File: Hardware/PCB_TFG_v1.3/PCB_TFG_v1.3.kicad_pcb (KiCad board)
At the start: 2 copper layers, 44.4 x 62 mm, 48 parts, among them J2 Conn_01x06_Pin, J3 770669-1, Q1 8MHz, Q3 NPN, U1 STM32H523CET6, U2 TCAN330, U3 MCP1755ST-3302E/DB

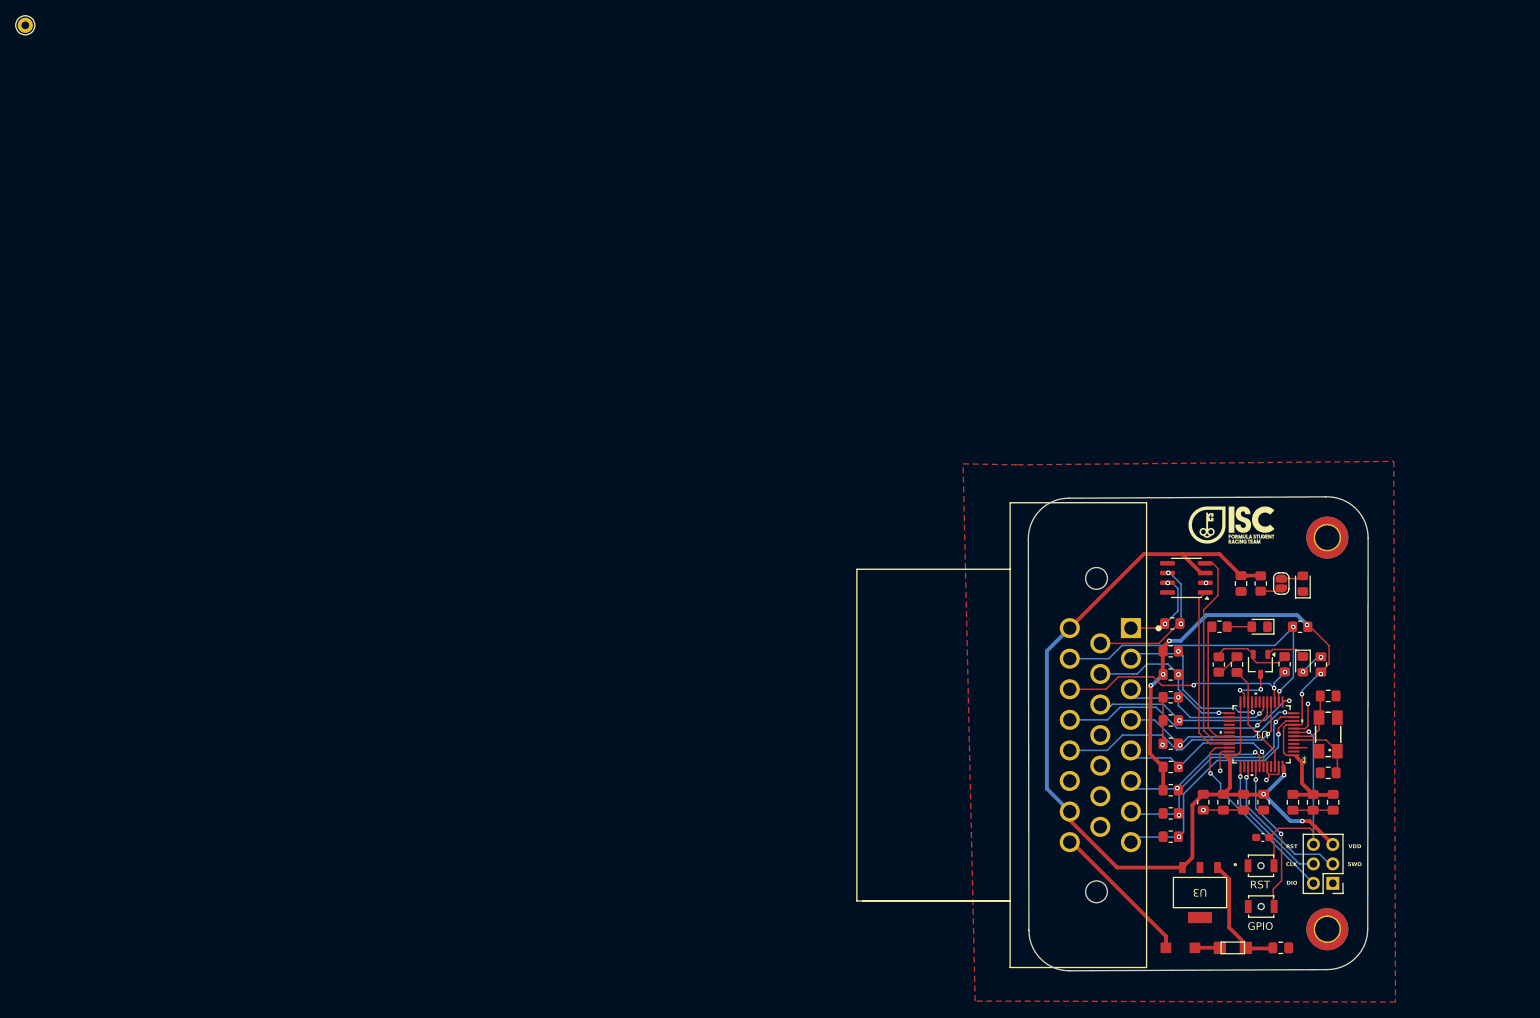
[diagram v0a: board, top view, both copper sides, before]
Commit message: MODIFICACIONES AL PCB
- Separación de Áreas Analógica y Digital.
- Creación de dos planos de GND y Vcc en capas intermedias.
- Recolocación de los C de desacoplo.
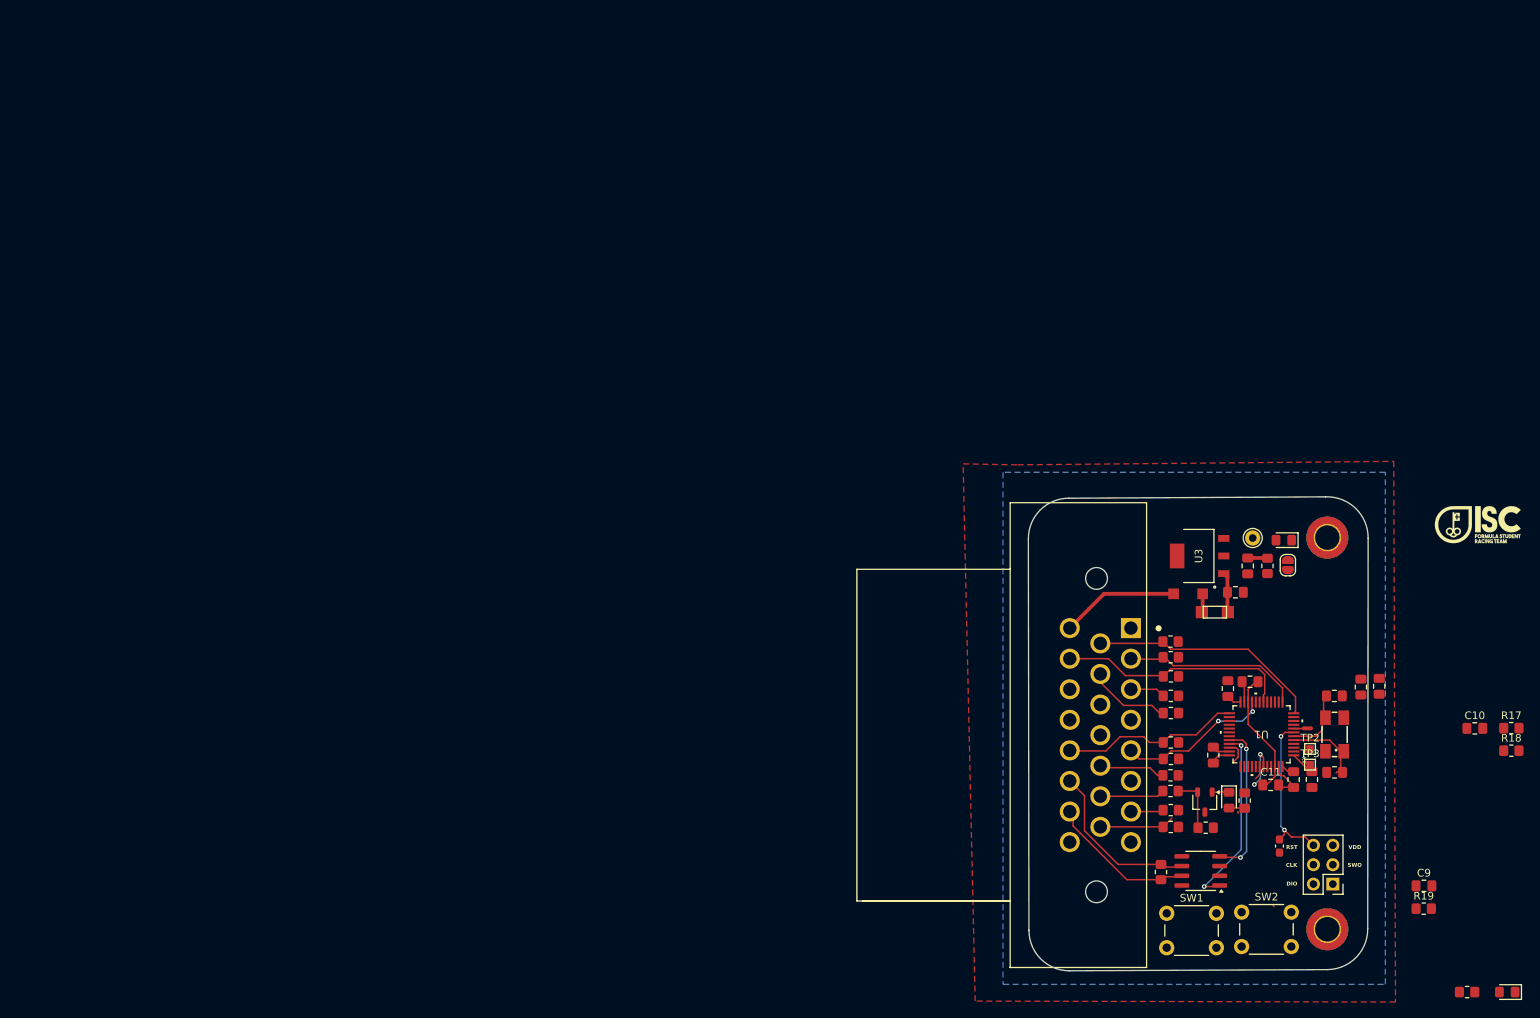
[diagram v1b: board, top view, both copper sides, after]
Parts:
- added C10: 2.2 uF, Capacitor_SMD:C_0805_2012Metric_Pad1.18x1.45mm_HandSolder, F.Cu at (201.7, 93.5)
- added C11: 2.2 uF, Capacitor_SMD:C_0805_2012Metric_Pad1.18x1.45mm_HandSolder, F.Cu at (175.0, 100.9)
- added NT1: NetTie_2, NetTie:NetTie-2_SMD_Pad0.5mm, F.Cu at (179.8, 93.5)
- added R17: 0, Resistor_SMD:R_0805_2012Metric_Pad1.20x1.40mm_HandSolder, F.Cu at (206.5, 93.5)
- added R18: 10k, Resistor_SMD:R_0805_2012Metric_Pad1.20x1.40mm_HandSolder, F.Cu at (206.5, 96.4)
- added R19: 100k, Resistor_SMD:R_0805_2012Metric_Pad1.20x1.40mm_HandSolder, F.Cu at (195.0, 117.1)
- added TP2: LSE_OSC_IN, TestPoint:TestPoint_Pad_1.0x1.0mm, F.Cu at (180.2, 96.2)
- added TP3: LSE_OSC_OUT, TestPoint:TestPoint_Pad_1.0x1.0mm, F.Cu at (180.2, 98.2)
- SW1: renamed from RST; footprint Button_Switch_SMD:SW_SPST_B3U-1000P-B -> Button_Switch_THT:SW_PUSH_6mm_H4.3mm
- SW2: renamed from GPIO; footprint Button_Switch_SMD:SW_SPST_B3U-1000P-B -> Button_Switch_THT:SW_PUSH_6mm_H4.3mm
- moved TP1 174.0 mm to (172.7, 68.6)
- moved D3 57.7 mm to (205.9, 128.0)
- moved R7 57.7 mm to (200.7, 128.0)
- moved C3 46.9 mm to (170.4, 75.7)
- moved D2 46.3 mm to (164.2, 75.9)
- moved U3 44.0 mm to (165.6, 71.0), turned to 90 degrees
- moved U$1 44.0 mm to (167.7, 78.3)
- moved U2 38.4 mm to (165.8, 112.2)
- moved R3 32.6 mm to (160.7, 112.3), turned to 90 degrees
- moved G*** 32.2 mm to (202.1, 66.8)
- moved C9 28.4 mm to (195.1, 114.1), turned to 0 degrees
- moved R16 25.8 mm to (161.9, 99.7)
- moved R12 22.3 mm to (161.9, 101.7), turned to 0 degrees
- moved R13 21.4 mm to (166.5, 106.5), turned to 0 degrees
- moved R14 20.4 mm to (171.6, 103.0), turned to 90 degrees
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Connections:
- C4 pad 2: GND -> unconnected-(C4-Pad2)
- C6 pad 2: VBAT -> VDDA
- C7 pad 2: VBAT -> VDDA
- D2 pad C: Net-(D2-PadC) -> unconnected-(D2-PadC)
- J3 pad 1: CANH1 -> GNDA
- J3 pad 10: TEMP_TYRE_2_SDA -> S_SUSP_FL
- J3 pad 11: APPS_2 -> unconnected-(J3-Pad11)
- J3 pad 13: unconnected-(J3-Pad13) -> TEMPS_BRK_CS
- J3 pad 14: unconnected-(J3-Pad14) -> TEMPS_BRK_SCK
- J3 pad 15: unconnected-(J3-Pad15) -> TEMP_TYRE_1_SDA
- J3 pad 16: VDD -> unconnected-(J3-Pad16)
- J3 pad 17: TEMPS_BRK_CS -> PRSS_BRK
- J3 pad 18: TEMPS_BRK_SCK -> unconnected-(J3-Pad18)
- J3 pad 19: TEMPS_BRK_MOSI -> unconnected-(J3-Pad19)
- J3 pad 2: TEMP_TYRE_2_SCL -> APPS_2
- J3 pad 20: TEMPS_BRK_MISO -> TEMP_TYRE_2_SDA
- J3 pad 21: unconnected-(J3-Pad21) -> CANL1
- J3 pad 22: VDD -> CANH1
- J3 pad 23: +12V -> VDD
- J3 pad 3: PRSS_BRK -> S_SUSP_FR
- J3 pad 4: APPS_1 -> TEMPS_BRK_MISO
- J3 pad 5: TEMP_TYRE_1_SDA -> TEMP_TYRE_2_SCL
- J3 pad 6: TEMP_TYRE_1_SCL -> TEMPS_BRK_MOSI
- J3 pad 7: S_SUSP_FR -> TEMP_TYRE_1_SCL
- J3 pad 8: S_SUSP_FL -> GND
- J3 pad 9: CANL1 -> APPS_1
- U$1 pad P$1: Net-(D2-PadC) -> unconnected-(U$1-PadP$1)
- U1 pad 3: unconnected-(U1-PC14-OSC32_IN-Pad3) -> Net-(U1-PC14-OSC32_IN)
- U1 pad 4: unconnected-(U1-PC15-OSC32_OUT-Pad4) -> Net-(U1-PC15-OSC32_OUT)
- U1 pad 44: GND -> Net-(SW3-B)
- U1 pad 46: Net-(C10-Pad1) -> Net-(C11-Pad1)
- U1 pad 8: GND -> GNDA
- U1 pad 9: VBAT -> VDDA
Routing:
- net VDD: track 128.3 -> 9.81 mm, vias 3 -> 0
- net VBAT: track 75.6 -> 2.95 mm, vias 6 -> 0
- net TEMPS_BRK_CS: track 41.6 -> 8.71 mm, vias 2 -> 0
- net TEMPS_BRK_MISO: track 32.8 -> 0.00 mm, vias 1 -> 0
- net TEMPS_BRK_MOSI: track 30.1 -> 0.00 mm, vias 1 -> 0
- net GND: track 40.6 -> 11.9 mm, vias 8 -> 0
- net S_SUSP_FR: track 31.3 -> 4.58 mm, vias 2 -> 0
- net TEMPS_BRK_SCK: track 34.0 -> 8.47 mm, vias 3 -> 0
- net SWDIO: track 26.0 -> 3.28 mm, vias 1 -> 0
- net S_SUSP_FL: track 33.6 -> 11.0 mm, vias 2 -> 0
- net GPIO: track 20.4 -> 0.18 mm, vias 2 -> 0
- net SWO: track 19.9 -> 0.00 mm, vias 1 -> 0
- net SWCLK: track 17.8 -> 0.51 mm, vias 1 -> 0
- net FLAG: track 16.7 -> 0.00 mm
- net TEMP_TYRE_1_SCL: track 21.7 -> 5.86 mm, vias 2 -> 0
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- added copper zone on B.Cu, net GND
- added copper zone on In2.Cu, net GND
- added copper zone on In1.Cu, net VDD
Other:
- copper layers 2 -> 4

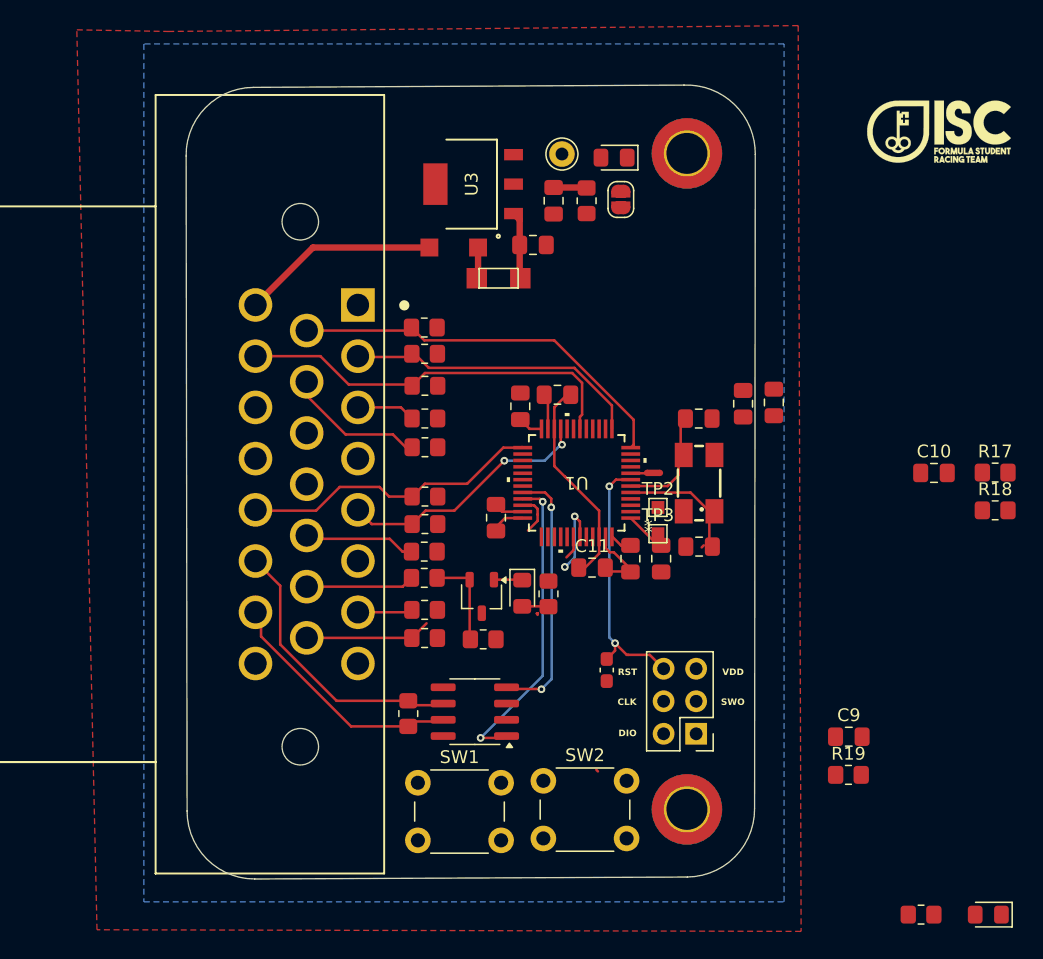
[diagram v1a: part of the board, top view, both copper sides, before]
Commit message: ENRUTADO COMPLETADO
- Nueva versión del PCB ya enrutado.
- Modificadas huellas de algunos componentes, principalmente para incluir marca de posición.
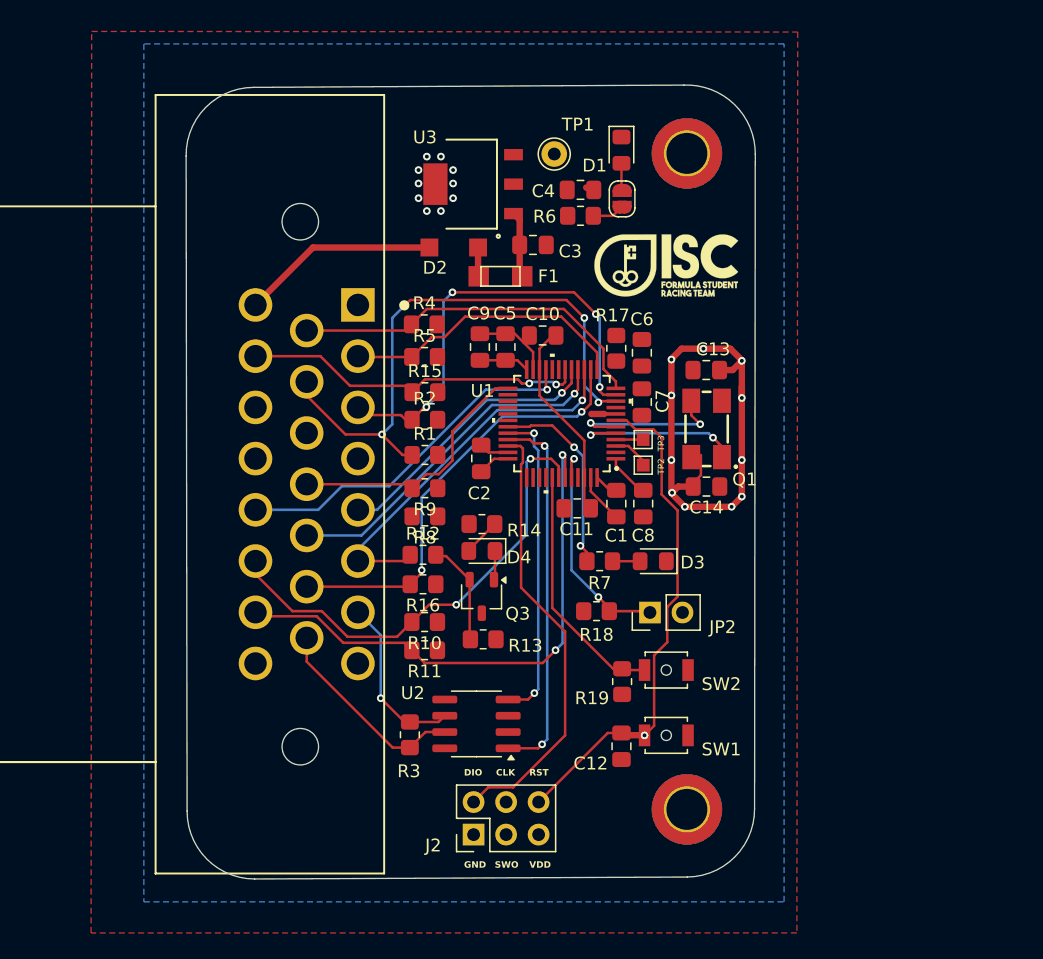
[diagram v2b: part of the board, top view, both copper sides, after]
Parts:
- removed the C10 at (172.3, 87.4)
- added JP2: Jumper_2_Open, Connector_PinHeader_2.54mm:PinHeader_1x02_P2.54mm_Vertical, F.Cu at (179.5, 104.4)
- C12: footprint Capacitor_SMD:C_0603_1608Metric_Pad1.08x0.95mm_HandSolder -> Capacitor_SMD:C_0805_2012Metric_Pad1.18x1.45mm_HandSolder
- SW1, SW2: footprint Button_Switch_THT:SW_PUSH_6mm_H4.3mm -> Button_Switch_SMD:SW_SPST_B3U-1000P-B
- moved C9 41.9 mm to (166.2, 83.7), turned to 90 degrees
- moved D3 38.0 mm to (179.8, 100.4)
- moved R7 37.3 mm to (175.6, 100.4)
- moved C10 32.4 mm to (171.1, 82.8), turned to 180 degrees
- moved R18 32.1 mm to (175.3, 104.3)
- moved R17 31.1 mm to (176.9, 83.8), turned to 90 degrees
- moved G*** 23.7 mm to (180.8, 77.3)
- moved SW1 19.7 mm to (180.8, 114.0), turned to 180 degrees
- moved R19 19.1 mm to (177.3, 109.8), turned to 90 degrees
- moved J2 19.1 mm to (165.8, 121.8), turned to 90 degrees
- moved SW2 12.9 mm to (180.8, 108.9), turned to 180 degrees
- moved C6 11.0 mm to (178.9, 84.1), turned to -90 degrees
- moved C7 7.91 mm to (178.9, 88.0)
- moved R14 7.53 mm to (166.4, 97.5), turned to 180 degrees
- moved TP3 7.44 mm to (179.0, 90.9)
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- renumbered U$1 to F1
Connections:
- C10 pad 1: Net-(C10-Pad1) -> VCAP
- C11 pad 1: Net-(C11-Pad1) -> VCAP
- C4 pad 2: unconnected-(C4-Pad2) -> GND
- C6 pad 1: GND -> GNDA
- C7 pad 1: GND -> GNDA
- D2 pad C: unconnected-(D2-PadC) -> Net-(D2-PadC)
- F1 pad P$1: unconnected-(U$1-PadP$1) -> Net-(D2-PadC)
- J3 pad 12: unconnected-(J3-Pad12) -> TEMP_TYRE_2_SDA
- J3 pad 13: TEMPS_BRK_CS -> TEMPS_BRK_MISO
- J3 pad 14: TEMPS_BRK_SCK -> TEMPS_BRK_CS
- J3 pad 15: TEMP_TYRE_1_SDA -> CANH1
- J3 pad 16: unconnected-(J3-Pad16) -> +12V
- J3 pad 20: TEMP_TYRE_2_SDA -> TEMP_TYRE_2_SCL
- J3 pad 21: CANL1 -> TEMP_TYRE_1_SCL
- J3 pad 22: CANH1 -> TEMP_TYRE_1_SDA
- J3 pad 4: TEMPS_BRK_MISO -> unconnected-(J3-Pad4)
- J3 pad 5: TEMP_TYRE_2_SCL -> TEMPS_BRK_MOSI
- J3 pad 6: TEMPS_BRK_MOSI -> TEMPS_BRK_SCK
- J3 pad 7: TEMP_TYRE_1_SCL -> CANL1
- U1 pad 22: Net-(C10-Pad1) -> VCAP
- U1 pad 46: Net-(C11-Pad1) -> VCAP
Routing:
- net GND: track 11.9 -> 53.6 mm, vias 0 -> 21
- net S_SUSP_FL: track 11.0 -> 45.3 mm, vias 0 -> 4
- net SWDIO: track 3.28 -> 34.4 mm
- net TEMP_TYRE_1_SCL: track 5.86 -> 36.9 mm, vias 0 -> 2
- net S_SUSP_FR: track 4.58 -> 35.3 mm, vias 0 -> 4
- net TEMPS_BRK_MISO: track 0.00 -> 27.9 mm, vias 0 -> 1
- net TEMP_TYRE_1_SDA: track 15.9 -> 43.4 mm
- net TEMPS_BRK_CS: track 8.71 -> 34.2 mm, vias 0 -> 2
- net TEMPS_BRK_MOSI: track 0.00 -> 21.9 mm, vias 0 -> 1
- net TEMPS_BRK_SCK: track 8.47 -> 30.0 mm, vias 0 -> 1
- net GPIO: track 0.18 -> 20.0 mm
- net NRST: track 20.4 -> 39.5 mm, vias 2 -> 1
- net Net-(JP2-A): track 0.00 -> 18.0 mm, vias 0 -> 2
- net VCAP: track 0.00 -> 16.3 mm
- net FLAG: track 0.00 -> 15.4 mm, vias 0 -> 2
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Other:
- board text added: "GND"
